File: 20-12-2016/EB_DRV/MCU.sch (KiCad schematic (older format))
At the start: 16 parts, among them U2 STM32F401RBT6, Y1 8MHz

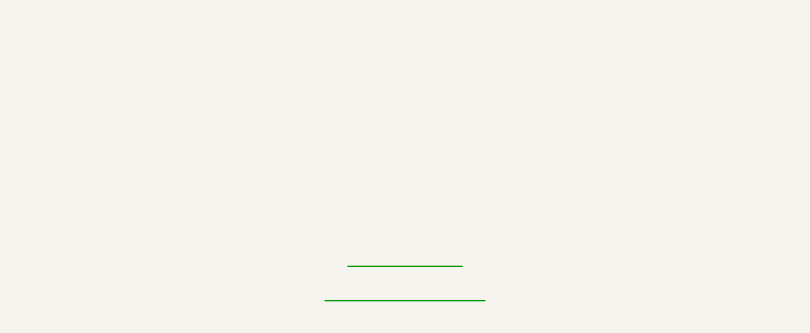
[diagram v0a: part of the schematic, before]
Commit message: Added_footprints(not all)
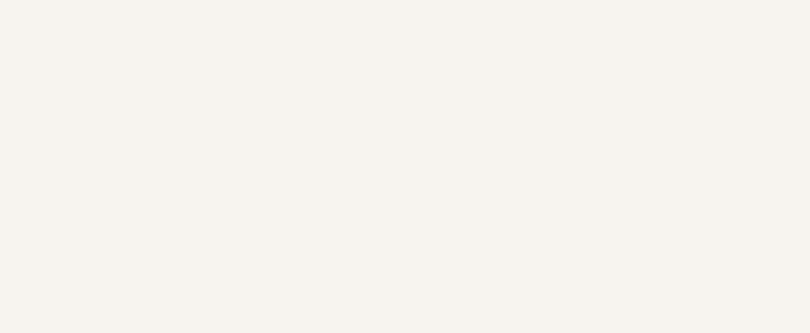
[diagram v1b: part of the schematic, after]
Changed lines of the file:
@@
 	5450 7300 5100 7300
-Wire Wire Line
-	2600 7400 3100 7400
-Wire Wire Line
-	2500 7550 3200 7550
 Wire Wire Line
 	5350 2700 5350 2600
